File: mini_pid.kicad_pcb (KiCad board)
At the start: 2 copper layers, 68.8 x 63.8 mm, 68 parts, among them P1 PD Mon/Output, P2 Ext. Mod/SetPt Mon, U1 ED2610, U2 OPA2211, U3 LM2940, U4 OPA4227, U5 8DIP, U6 8DIP, U7 OPA2227

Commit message: Layout for old version completed
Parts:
- removed P2: Ext. Mod/SetPt Mon, footprints:Dual-BNC-ARF2136
- added REF**: Via-0.6mm, footprints:Via-0.6mm, F.Cu at (112.8, 72.8)
- added REF**: Via-0.6mm, footprints:Via-0.6mm, F.Cu at (110.7, 103.8)
- added REF**: Via-0.6mm, footprints:Via-0.6mm, F.Cu at (121.8, 90.3)
- added REF**: Via-0.6mm, footprints:Via-0.6mm, F.Cu at (108.6, 98.0)
- added REF**: Via-0.6mm, footprints:Via-0.6mm, F.Cu at (109.9, 98.0)
- added REF**: Via-0.6mm, footprints:Via-0.6mm, F.Cu at (111.4, 99.3)
- added REF**: Via-0.6mm, footprints:Via-0.6mm, F.Cu at (122.9, 92.3)
- added REF**: Via-0.6mm, footprints:Via-0.6mm, F.Cu at (121.9, 94.3)
- added REF**: Via-0.6mm, footprints:Via-0.6mm, F.Cu at (109.5, 90.2)
- added REF**: Via-0.6mm, footprints:Via-0.6mm, F.Cu at (108.8, 93.7)
- added REF**: Via-0.6mm, footprints:Via-0.6mm, F.Cu at (117.0, 85.1)
- added REF**: Via-0.6mm, footprints:Via-0.6mm, F.Cu at (112.3, 70.1)
- added REF**: Via-0.6mm, footprints:Via-0.6mm, F.Cu at (115.8, 85.1)
- added REF**: Via-0.6mm, footprints:Via-0.6mm, F.Cu at (78.9, 90.0)
- added REF**: Via-0.6mm, footprints:Via-0.6mm, F.Cu at (113.2, 69.1)
- added REF**: Via-0.6mm, footprints:Via-0.6mm, F.Cu at (97.0, 100.0)
- added REF**: Via-0.6mm, footprints:Via-0.6mm, F.Cu at (97.7, 99.1)
- added REF**: Via-0.6mm, footprints:Via-0.6mm, F.Cu at (95.9, 99.2)
- added REF**: Via-0.6mm, footprints:Via-0.6mm, F.Cu at (87.8, 96.2)
- added REF**: Via-0.6mm, footprints:Via-0.6mm, F.Cu at (87.6, 97.4)
- added REF**: Via-0.6mm, footprints:Via-0.6mm, F.Cu at (112.0, 103.8)
- added S3: spdt, footprints:CJS-1200TB-SPDT, B.Cu at (120.1, 116.0)
- moved R22 10.8 mm to (114.5, 112.0), turned to 270 degrees
- moved S2 10.6 mm to (129.4, 101.3)
- moved R20 6.00 mm to (113.1, 108.1)
- moved R24 5.73 mm to (131.4, 105.1)
- moved C18 4.58 mm to (125.7, 105.4), turned to 180 degrees
- moved R4 4.51 mm to (127.1, 109.0)
- moved R7 4.28 mm to (124.6, 109.1)
- moved R23 4.27 mm to (125.5, 102.1), turned to 270 degrees
- moved R5 3.57 mm to (129.1, 105.9), turned to 270 degrees
- moved C29 1.31 mm to (89.0, 97.2), turned to 270 degrees
- moved R18 1.21 mm to (87.8, 93.9)
- moved S1 1.20 mm to (110.7, 112.5)
- moved U4 0.59 mm to (119.5, 105.5)
- moved C19 0.28 mm to (113.0, 105.5), turned to 0 degrees
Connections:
- R4 pad 1: Net-(P2-Pad1) -> /ext.mod.input
- U2 pad 9: (no net) -> GND
- U4 pad 1: Net-(R22-Pad2) -> Net-(S3-Pad1)
- U4 pad 2: Net-(R20-Pad2) -> Net-(S3-Pad1)
- U4 pad 3: GND -> Net-(C15-Pad1)
- U4 pad 5: Net-(C15-Pad1) -> GND
- U4 pad 6: Net-(P1-Pad1) -> Net-(R20-Pad2)
- U4 pad 7: Net-(P1-Pad1) -> Net-(R22-Pad2)
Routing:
- net -15V: track 86.2 -> 137.5 mm, vias 4 -> 5
- net Net-(R21-Pad1): track 0.00 -> 41.6 mm, vias 0 -> 1
- net Net-(R18-Pad1): track 3.57 -> 35.4 mm, vias 0 -> 1
- net Net-(R7-Pad2): track 0.00 -> 30.9 mm, vias 0 -> 2
- net /5V: track 0.00 -> 29.5 mm
- net Net-(C11-Pad1): track 0.00 -> 29.5 mm
- net +15V: track 46.9 -> 75.5 mm, vias 0 -> 2
- net Net-(C27-Pad1): track 4.60 -> 31.4 mm
- net Net-(P1-Pad1): track 0.00 -> 25.7 mm
- net Net-(C15-Pad1): track 8.94 -> 32.4 mm
- net Net-(R17-Pad1): track 44.5 -> 59.7 mm
- net Net-(S3-Pad1): track 0.00 -> 14.9 mm, vias 0 -> 1
- net Net-(C20-Pad1): track 34.3 -> 47.5 mm
- net Net-(R6-Pad1): track 33.1 -> 45.8 mm
- net Net-(R10-Pad2): track 31.2 -> 43.9 mm
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- added copper zone on B.Cu, net GND
- added copper zone on F.Cu, net GND
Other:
- board size 68.8 x 63.8 mm -> 67.1 x 63.8 mm

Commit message: Reset board layout
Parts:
- removed REF** (x21): Via-0.6mm, footprints:Via-0.6mm
- added C1: 10uF, Capacitors_SMD:C_0805_HandSoldering, F.Cu at (384.1, 40.0)
- added C31: 1000pF, Capacitors_SMD:C_0805_HandSoldering, F.Cu at (299.2, 145.5)
- added C32: 4700pF, Capacitors_SMD:C_0805_HandSoldering, F.Cu at (307.1, 132.7)
- added C33: 0.022uF, Capacitors_SMD:C_0805_HandSoldering, F.Cu at (323.5, 130.3)
- added C34: 10uF, Capacitors_SMD:C_0805_HandSoldering, F.Cu at (291.2, 155.1)
- added C35: 0.1uF, Capacitors_SMD:C_0805_HandSoldering, F.Cu at (296.8, 151.1)
- added D3: TL4050B51, TO_SOT_Packages_SMD:SOT-23, F.Cu at (264.3, 150.0)
- added D4: TL4050B51, TO_SOT_Packages_SMD:SOT-23, F.Cu at (273.1, 150.0)
- added J1: DB9, footprints:DB9_Throughhole, F.Cu at (397.3, 17.1)
- added P2: Output/Monitor, footprints:Dual-BNC-ARF2136, F.Cu at (343.4, 40.0)
- added P3: Servo In/Ext. Mod, footprints:Dual-BNC-ARF2136, F.Cu at (327.7, 114.3)
- added P4: Output/Monitor, footprints:Dual-BNC-ARF2136, F.Cu at (342.7, 114.3)
- added R25: 10k, Resistors_SMD:R_0805_HandSoldering, F.Cu at (306.6, 138.2)
- added R26: 10k, Resistors_SMD:R_0805_HandSoldering, F.Cu at (311.8, 138.2)
- added R27: 1k, Resistors_SMD:R_0805_HandSoldering, F.Cu at (316.9, 138.2)
- added R28: 10k, Resistors_SMD:R_0805_HandSoldering, F.Cu at (310.5, 143.8)
- added R29: 1k, Resistors_SMD:R_0805_HandSoldering, F.Cu at (327.2, 141.4)
- added R30: 100k, Resistors_SMD:R_0805_HandSoldering, F.Cu at (315.6, 143.8)
- added R31: 10k, Resistors_SMD:R_0805_HandSoldering, F.Cu at (301.8, 151.1)
- added R32: 1k, Resistors_SMD:R_0805_HandSoldering, F.Cu at (322.1, 135.9)
- added R33: 100, Resistors_SMD:R_0805_HandSoldering, F.Cu at (332.4, 135.2)
- added R34: 33k, Resistors_SMD:R_0805_HandSoldering, F.Cu at (322.1, 141.4)
- added R35: 3.3k, Resistors_SMD:R_0805_HandSoldering, F.Cu at (327.2, 135.9)
- added R36: 330, Resistors_SMD:R_0805_HandSoldering, F.Cu at (320.8, 147.0)
- added R37: 12, Resistors_SMD:R_0805_HandSoldering, F.Cu at (312.5, 149.3)
- added R38: 10k, Resistors_SMD:R_0805_HandSoldering, F.Cu at (312.5, 154.9)
- added R39: 1k, Resistors_SMD:R_0805_HandSoldering, F.Cu at (307.0, 155.6)
- added R40: 1k, Resistors_SMD:R_0805_HandSoldering, F.Cu at (317.7, 152.5)
- added R41: 10k, Resistors_SMD:R_0805_HandSoldering, F.Cu at (322.8, 152.5)
- added R42: 10k, Resistors_SMD:R_0805_HandSoldering, F.Cu at (328.0, 147.0)
- added R43: 1k, Resistors_SMD:R_0805_HandSoldering, F.Cu at (338.3, 130.3)
- added R44: 12, Resistors_SMD:R_0805_HandSoldering, F.Cu at (333.1, 140.8)
- added RV3: 10k, footprints:VishaySpectrol536, F.Cu at (263.6, 49.8)
- added RV4: 1k, footprints:VishaySpectrol536, F.Cu at (309.1, 101.3)
- added RV5: 1k, footprints:VishaySpectrol536, F.Cu at (286.4, 101.3)
- added RV6: 10k, footprints:VishaySpectrol536, F.Cu at (263.6, 101.3)
- added S4: spdt, footprints:SPDT-Horizontal, F.Cu at (321.2, 43.2)
- added S5: spdt, footprints:SPDT-Horizontal, F.Cu at (370.1, 94.7)
- added S6: spdt, footprints:SPDT-Horizontal, F.Cu at (356.9, 94.7)
- added S7: spdt, footprints:SPDT-Horizontal, F.Cu at (356.9, 128.2)
- added S8: spdt, footprints:SPDT-Horizontal, F.Cu at (370.1, 128.2)
- added U8: 8DIP, footprints:8_POS_DIP_Switch, F.Cu at (254.2, 139.8)
- added U9: 8DIP, footprints:8_POS_DIP_Switch, F.Cu at (276.4, 139.8)
- C10, C22, C5, C7, C9: footprint Capacitors_SMD:C_0603_HandSoldering -> Capacitors_SMD:C_0805_HandSoldering
- C11, C3, C4: value 10uF -> 0.1uF; footprint Capacitors_SMD:C_0603_HandSoldering -> Capacitors_SMD:C_0805_HandSoldering
- C12: value 0.1uF -> 330pF; footprint Capacitors_SMD:C_0603_HandSoldering -> Capacitors_SMD:C_0805_HandSoldering
- C13, C28: value 0.1uF -> 2200pf; footprint Capacitors_SMD:C_0603_HandSoldering -> Capacitors_SMD:C_0805_HandSoldering
- C14: value 10uF -> 10000pF; footprint Capacitors_SMD:C_0603_HandSoldering -> Capacitors_SMD:C_0805_HandSoldering
- C15: value 15pF -> 0.047uF; footprint Capacitors_SMD:C_0603_HandSoldering -> Capacitors_SMD:C_0805_HandSoldering
- C16: value 22uF -> 1000pF; footprint SMD_Packages:SMD-2512_Pol -> Capacitors_SMD:C_0805_HandSoldering
- C17: value 0.1uF -> 4700pF; footprint Capacitors_SMD:C_0603_HandSoldering -> Capacitors_SMD:C_0805_HandSoldering
- C18: value 0.1uF -> 0.022uF; footprint Capacitors_SMD:C_0603_HandSoldering -> Capacitors_SMD:C_0805_HandSoldering
- C19, C2, C6: value 0.1uF -> 10uF; footprint Capacitors_SMD:C_0603_HandSoldering -> Capacitors_SMD:C_0805_HandSoldering
- C20: value 3.3nF -> 0.1uF; footprint Capacitors_SMD:C_0603_HandSoldering -> Capacitors_SMD:C_0805_HandSoldering
- C21: value 22nF -> 10uF; footprint Capacitors_SMD:C_0603_HandSoldering -> Capacitors_SMD:C_0805_HandSoldering
- C23: value 0.47uF -> 0.1uF; footprint Capacitors_SMD:C_0603_HandSoldering -> Capacitors_SMD:C_0805_HandSoldering
- C24: value 10nF -> 0.1uF; footprint Capacitors_SMD:C_0603_HandSoldering -> Capacitors_SMD:C_0805_HandSoldering
- C25: value 47nF -> 0.1uF; footprint Capacitors_SMD:C_0603_HandSoldering -> Capacitors_SMD:C_0805_HandSoldering
- C26: value 0.22uF -> 0.1uF; footprint Capacitors_SMD:C_0603_HandSoldering -> Capacitors_SMD:C_0805_HandSoldering
- C27: value 10uF -> 330pF; footprint Capacitors_SMD:C_0603_HandSoldering -> Capacitors_SMD:C_0805_HandSoldering
- C29: value 0.1uF -> 10000pF; footprint Capacitors_SMD:C_0603_HandSoldering -> Capacitors_SMD:C_0805_HandSoldering
- C30: value 0.1uF -> 0.047uF; footprint Capacitors_SMD:C_0603_HandSoldering -> Capacitors_SMD:C_0805_HandSoldering
- C8: value 15pF -> 0.1uF; footprint Capacitors_SMD:C_0603_HandSoldering -> Capacitors_SMD:C_0805_HandSoldering
- D1: value S5971 -> TL4050B51; footprint footprints:S5971 -> TO_SOT_Packages_SMD:SOT-23
- P1: value PD Mon/Output -> Servo In/Ext. Mod
- R1: value 3.3k -> 750; footprint Resistors_SMD:R_0603_HandSoldering -> Resistors_SMD:R_0805_HandSoldering
- R10, R21, R5, R7: value 10k -> 1k; footprint Resistors_SMD:R_0603_HandSoldering -> Resistors_SMD:R_0805_HandSoldering
- R11: value 1k -> 100; footprint Resistors_SMD:R_0603_HandSoldering -> Resistors_SMD:R_0805_HandSoldering
- R12: value 100 -> 33k; footprint Resistors_SMD:R_0603_HandSoldering -> Resistors_SMD:R_0805_HandSoldering
- R13: value 33k -> 3.3k; footprint Resistors_SMD:R_0603_HandSoldering -> Resistors_SMD:R_0805_HandSoldering
- R14: value 3.3k -> 330; footprint Resistors_SMD:R_0603_HandSoldering -> Resistors_SMD:R_0805_HandSoldering
- R15: value 330 -> 12; footprint Resistors_SMD:R_0603_HandSoldering -> Resistors_SMD:R_0805_HandSoldering
- R16: value 12 -> 10k; footprint Resistors_SMD:R_0603_HandSoldering -> Resistors_SMD:R_0805_HandSoldering
- R17, R18, R4: footprint Resistors_SMD:R_0603_HandSoldering -> Resistors_SMD:R_0805_HandSoldering
- R19, R20, R6: value 1k -> 10k; footprint Resistors_SMD:R_0603_HandSoldering -> Resistors_SMD:R_0805_HandSoldering
- R2: value 100 -> 750; footprint Resistors_SMD:R_0603_HandSoldering -> Resistors_SMD:R_0805_HandSoldering
- R22: value 1k -> 12; footprint Resistors_SMD:R_0603_HandSoldering -> Resistors_SMD:R_0805_HandSoldering
- R23: value 1k -> 750; footprint Resistors_SMD:R_0603_HandSoldering -> Resistors_SMD:R_0805_HandSoldering
- R24: value 12 -> 750; footprint Resistors_SMD:R_0603_HandSoldering -> Resistors_SMD:R_0805_HandSoldering
- R3: value 3.3k -> 10k; footprint Resistors_SMD:R_0603_HandSoldering -> Resistors_SMD:R_0805_HandSoldering
- R8: value 1k -> 100k; footprint Resistors_SMD:R_0603_HandSoldering -> Resistors_SMD:R_0805_HandSoldering
- R9: value 100k -> 10k; footprint Resistors_SMD:R_0603_HandSoldering -> Resistors_SMD:R_0805_HandSoldering
- RV2: value 10k -> 1k; footprint footprints:Bourns-PV36W104C01B00-trimmer -> footprints:VishaySpectrol536
- S1, S2, S3: footprint footprints:CJS-1200TB-SPDT -> footprints:SPDT-Horizontal
- U2: value OPA2211 -> OPA4227; footprint Housings_SOIC:SOIC-8-1EP_3.9x4.9mm_Pitch1.27mm -> Housings_SOIC:SOIC-14_3.9x8.7mm_Pitch1.27mm
- U3: value LM2940 -> OPA2227; footprint TO_SOT_Packages_SMD:SOT-223 -> Housings_SOIC:SOIC-8_3.9x4.9mm_Pitch1.27mm
- U4: value OPA4227 -> 8DIP; footprint Housings_SOIC:SOIC-14_3.9x8.7mm_Pitch1.27mm -> footprints:8_POS_DIP_Switch
- U6: value 8DIP -> OPA4227; footprint footprints:8_POS_DIP_Switch -> Housings_SOIC:SOIC-14_3.9x8.7mm_Pitch1.27mm
- moved U1 306.1 mm to (422.8, 18.2)
- moved C2 302.5 mm to (415.4, 25.9)
- moved C5 279.6 mm to (399.3, 39.6)
- moved C9 279.2 mm to (375.5, 21.9)
- moved R12 278.4 mm to (365.2, 44.1)
- moved C19 277.3 mm to (375.5, 16.3)
- moved R10 276.3 mm to (372.2, 37.6)
- moved R6 275.7 mm to (371.9, 43.0)
- moved C3 275.6 mm to (389.0, 40.0)
- moved R16 275.3 mm to (359.7, 45.5)
- moved R17 274.3 mm to (364.6, 50.9)
- moved R18 274.1 mm to (359.3, 56.1)
- moved C4 270.0 mm to (394.0, 40.0)
- moved R11 266.8 mm to (359.4, 50.6)
- moved C8 265.4 mm to (372.2, 32.5)
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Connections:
- C11 pad 1: Net-(C11-Pad1) -> GND
- C11 pad 2: GND -> +15V
- C12 pad 1: +15V -> Net-(C12-Pad1)
- C12 pad 2: GND -> Net-(C12-Pad2)
- C13 pad 1: Net-(C11-Pad1) -> Net-(C12-Pad1)
- C13 pad 2: GND -> Net-(C13-Pad2)
- C14 pad 1: +15V -> Net-(C12-Pad1)
- C14 pad 2: GND -> Net-(C14-Pad2)
- C15 pad 1: Net-(C15-Pad1) -> Net-(C12-Pad1)
- C16 pad 1: +9V -> Net-(C12-Pad1)
- C16 pad 2: GND -> Net-(C16-Pad2)
- C17 pad 1: +9V -> Net-(C12-Pad1)
- C17 pad 2: GND -> Net-(C17-Pad2)
- C18 pad 1: GND -> Net-(C12-Pad1)
- C18 pad 2: -15V -> Net-(C18-Pad2)
- C19 pad 1: GND -> Net-(C19-Pad1)
- C19 pad 2: +15V -> /PI Circuit 1/-5V
- C2 pad 1: +9V -> GND
- C2 pad 2: GND -> -15V
- C20 pad 1: Net-(C20-Pad1) -> Net-(C19-Pad1)
- C20 pad 2: Net-(C20-Pad2) -> /PI Circuit 1/-5V
- C21 pad 1: Net-(C20-Pad1) -> /PI Circuit 2/set_point
- C21 pad 2: Net-(C21-Pad2) -> GND
- C22 pad 1: Net-(C20-Pad1) -> /PI Circuit 2/set_point
- C22 pad 2: Net-(C22-Pad2) -> GND
- C23 pad 1: Net-(C20-Pad1) -> GND
- C23 pad 2: Net-(C23-Pad2) -> -15V
- C24 pad 1: Net-(C20-Pad1) -> GND
- C24 pad 2: Net-(C24-Pad2) -> -15V
- C25 pad 1: Net-(C20-Pad1) -> GND
- C25 pad 2: Net-(C25-Pad2) -> +15V
- C26 pad 1: Net-(C20-Pad1) -> GND
- C26 pad 2: Net-(C26-Pad2) -> +15V
- C27 pad 2: GND -> Net-(C27-Pad2)
- C28 pad 2: GND -> Net-(C28-Pad2)
- C29 pad 1: GND -> Net-(C27-Pad1)
- C29 pad 2: -15V -> Net-(C29-Pad2)
- C3 pad 1: +15V -> Net-(C3-Pad1)
- C30 pad 1: GND -> Net-(C27-Pad1)
- C30 pad 2: +15V -> Net-(C30-Pad2)
- C4 pad 1: GND -> +15V
- C4 pad 2: -15V -> Net-(C3-Pad1)
- C5 pad 1: Net-(C5-Pad1) -> Net-(C3-Pad1)
- C5 pad 2: GND -> -15V
- C6 pad 1: +15V -> /PI Circuit 1/set_point
- C6 pad 2: Net-(C5-Pad1) -> GND
- C7 pad 1: Net-(C5-Pad1) -> /PI Circuit 1/set_point
- C7 pad 2: -15V -> GND
- C8 pad 1: Net-(C8-Pad1) -> GND
- C8 pad 2: Net-(C8-Pad2) -> -15V
- D1 pad 1: +9V -> /PI Circuit 1/+5V
- D1 pad 3: Net-(C8-Pad2) -> (no net)
- D2 pad 1: /5V -> GND
- D2 pad 2: GND -> /PI Circuit 1/-5V
- R1 pad 1: Net-(C8-Pad1) -> +15V
- R1 pad 2: Net-(C8-Pad2) -> /PI Circuit 1/+5V
- R16 pad 2: Net-(R10-Pad2) -> Net-(R16-Pad2)
- R17 pad 2: Net-(R10-Pad2) -> Net-(R17-Pad2)
- R18 pad 1: Net-(R18-Pad1) -> Net-(R17-Pad2)
- R18 pad 2: Net-(C20-Pad1) -> Net-(R18-Pad2)
- R19 pad 1: +15V -> Net-(R17-Pad1)
- R19 pad 2: /5V -> Net-(C12-Pad1)
- R2 pad 1: Net-(C15-Pad2) -> /PI Circuit 1/-5V
- R2 pad 2: Net-(C8-Pad1) -> -15V
- R20 pad 1: Net-(R18-Pad1) -> Net-(R20-Pad1)
- R21 pad 1: Net-(R21-Pad1) -> Net-(R20-Pad2)
- R22 pad 1: Net-(R20-Pad2) -> Net-(P2-Pad1)
- R22 pad 2: Net-(R22-Pad2) -> Net-(R21-Pad2)
- R23 pad 1: Net-(R21-Pad2) -> +15V
- R23 pad 2: Net-(R23-Pad2) -> /PI Circuit 2/+5V
- R24 pad 1: Net-(R24-Pad1) -> /PI Circuit 2/-5V
- R24 pad 2: Net-(P1-Pad3) -> -15V
- R3 pad 1: Net-(C15-Pad1) -> Net-(P1-Pad3)
- R3 pad 2: Net-(C15-Pad2) -> Net-(R3-Pad2)
- R4 pad 1: /ext.mod.input -> /PI Circuit 1/set_point
- R4 pad 2: Net-(R4-Pad2) -> Net-(R3-Pad2)
- R5 pad 1: Net-(C11-Pad1) -> Net-(R5-Pad1)
- R5 pad 2: Net-(R4-Pad2) -> Net-(P1-Pad1)
- R6 pad 1: Net-(R6-Pad1) -> Net-(R3-Pad2)
- R6 pad 2: Net-(C15-Pad1) -> /PI Circuit 1/set_point
- R7 pad 1: Net-(R4-Pad2) -> /PI Circuit 1/set_point
- R7 pad 2: Net-(R7-Pad2) -> Net-(R5-Pad1)
- R8 pad 1: Net-(R7-Pad2) -> Net-(R8-Pad1)
- R8 pad 2: Net-(R6-Pad1) -> Net-(R10-Pad2)
- RV1 pad 1: GND -> /PI Circuit 1/-5V
- RV1 pad 2: Net-(C11-Pad1) -> /PI Circuit 1/set_point
- RV1 pad 3: /5V -> /PI Circuit 1/+5V
- RV2 pad 2: Net-(C27-Pad1) -> Net-(R16-Pad1)
- RV2 pad 3: /5V -> Net-(R10-Pad2)
- S1 pad 1: Net-(R22-Pad2) -> Net-(P1-Pad1)
- S1 pad 2: Net-(R21-Pad1) -> Net-(S1-Pad2)
- S1 pad 3: Net-(R18-Pad1) -> /PI Circuit 1/set_point
- S2 pad 1: Net-(R23-Pad2) -> (no net)
- S2 pad 2: Net-(R24-Pad1) -> Net-(C12-Pad1)
- S2 pad 3: Net-(R21-Pad1) -> Net-(R16-Pad2)
- S3 pad 1: Net-(S3-Pad1) -> Net-(R18-Pad2)
- S3 pad 2: Net-(P1-Pad1) -> Net-(S3-Pad2)
- S3 pad 3: /ext.mod.input -> Net-(R17-Pad1)
- U2 pad 1: Net-(C15-Pad1) -> /PI Circuit 1/set_point
- U2 pad 2: Net-(C15-Pad2) -> Net-(R3-Pad2)
- U2 pad 4: -15V -> +15V
- U2 pad 5: GND -> Net-(S1-Pad2)
- U2 pad 6: Net-(C8-Pad2) -> Net-(P2-Pad3)
- U2 pad 7: Net-(C8-Pad1) -> Net-(P2-Pad3)
- U2 pad 8: +15V -> Net-(R18-Pad2)
- U2 pad 9: GND -> Net-(R17-Pad2)
- U3 pad 1: +15V -> Net-(R10-Pad2)
- U3 pad 2: GND -> Net-(R5-Pad1)
- U3 pad 3: +9V -> GND
- U3 pad 4: GND -> -15V
- U4 pad 1: Net-(S3-Pad1) -> Net-(R5-Pad1)
- U4 pad 10: GND -> Net-(R11-Pad1)
- U4 pad 11: -15V -> Net-(R14-Pad1)
- U4 pad 12: Net-(C27-Pad1) -> Net-(R10-Pad1)
- U4 pad 13: Net-(R21-Pad2) -> Net-(R13-Pad1)
- U4 pad 14: Net-(R23-Pad2) -> Net-(R9-Pad1)
- U4 pad 2: Net-(S3-Pad1) -> Net-(R5-Pad1)
- U4 pad 3: Net-(C15-Pad1) -> Net-(R5-Pad1)
- U4 pad 4: +15V -> Net-(R5-Pad1)
- U4 pad 5: GND -> Net-(R5-Pad1)
- U4 pad 6: Net-(R20-Pad2) -> Net-(R5-Pad1)
- U4 pad 7: Net-(R22-Pad2) -> Net-(R5-Pad1)
- U4 pad 8: Net-(R7-Pad2) -> Net-(R5-Pad1)
- U4 pad 9: Net-(R4-Pad2) -> Net-(R15-Pad1)
- U5 pad 1: Net-(R6-Pad1) -> Net-(R16-Pad2)
- U5 pad 10: Net-(R12-Pad1) -> Net-(C15-Pad2)
- U5 pad 11: Net-(R15-Pad1) -> Net-(C18-Pad2)
- U5 pad 12: Net-(R11-Pad1) -> Net-(C14-Pad2)
- U5 pad 13: Net-(R14-Pad1) -> Net-(C17-Pad2)
- U5 pad 14: Net-(R10-Pad1) -> Net-(C13-Pad2)
- U5 pad 15: Net-(R13-Pad1) -> Net-(C16-Pad2)
- U5 pad 16: Net-(R9-Pad1) -> Net-(C12-Pad2)
- U5 pad 2: Net-(R6-Pad1) -> Net-(R16-Pad2)
- U5 pad 3: Net-(R6-Pad1) -> Net-(R16-Pad2)
- U5 pad 4: Net-(R6-Pad1) -> Net-(R16-Pad2)
- U5 pad 5: Net-(R6-Pad1) -> Net-(R16-Pad2)
- U5 pad 6: Net-(R6-Pad1) -> Net-(R16-Pad2)
- U5 pad 7: Net-(R6-Pad1) -> Net-(R16-Pad2)
- U5 pad 8: Net-(R6-Pad1) -> Net-(R16-Pad2)
- U5 pad 9: Net-(R16-Pad1) -> Net-(C12-Pad1)
- U6 pad 1: Net-(R17-Pad1) -> /PI Circuit 2/set_point
- U6 pad 10: Net-(C23-Pad2) -> GND
- U6 pad 11: Net-(C26-Pad2) -> -15V
- U6 pad 12: Net-(C22-Pad2) -> Net-(C34-Pad1)
- U6 pad 13: Net-(C25-Pad2) -> Net-(R42-Pad2)
- U6 pad 14: Net-(C21-Pad2) -> Net-(R43-Pad2)
- U6 pad 2: Net-(R17-Pad1) -> Net-(R25-Pad2)
- U6 pad 3: Net-(R17-Pad1) -> GND
- U6 pad 4: Net-(R17-Pad1) -> +15V
- U6 pad 5: Net-(R17-Pad1) -> Net-(S5-Pad2)
- U6 pad 6: Net-(R17-Pad1) -> Net-(P4-Pad3)
- U6 pad 7: Net-(R17-Pad1) -> Net-(P4-Pad3)
- U6 pad 8: Net-(R17-Pad1) -> Net-(R40-Pad2)
- U6 pad 9: Net-(C20-Pad1) -> Net-(R39-Pad2)
- U7 pad 1: Net-(R18-Pad1) -> Net-(R30-Pad2)
- U7 pad 2: Net-(R17-Pad1) -> Net-(R27-Pad1)
- U7 pad 6: Net-(R6-Pad1) -> Net-(R38-Pad2)
- U7 pad 7: Net-(R10-Pad2) -> Net-(R39-Pad1)
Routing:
- net -15V: track 137.5 -> 0.00 mm, vias 5 -> 0
- net +15V: track 75.5 -> 0.00 mm, vias 2 -> 0
- net Net-(R17-Pad1): track 59.7 -> 0.00 mm, vias 2 -> 0
- net Net-(C20-Pad1): track 47.5 -> 0.00 mm, vias 1 -> 0
- net Net-(R6-Pad1): track 45.8 -> 0.00 mm, vias 1 -> 0
- net Net-(R10-Pad2): track 43.9 -> 0.00 mm
- net Net-(R21-Pad1): track 41.6 -> 0.00 mm, vias 1 -> 0
- net Net-(R18-Pad1): track 35.4 -> 0.00 mm, vias 1 -> 0
- net Net-(C15-Pad1): track 32.4 -> 0.00 mm
- net Net-(C27-Pad1): track 31.4 -> 0.00 mm
- net Net-(R7-Pad2): track 30.9 -> 0.00 mm, vias 2 -> 0
- net /5V: track 29.5 -> 0.00 mm
- net Net-(C11-Pad1): track 29.5 -> 0.00 mm
- net Net-(P1-Pad1): track 25.7 -> 0.00 mm
- net +9V: track 17.9 -> 0.00 mm, vias 2 -> 0
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- removed copper zone on B.Cu, net GND
- removed copper zone on F.Cu, net GND
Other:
- board outline removed
- board text removed: "+15"
- board text removed: "-15"

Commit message: Board connectors placed
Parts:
- C17, P1, R24, RV1, RV2, U1, U5, U6: moved to F.Cu
- S3: footprint footprints:SPDT-Horizontal -> footprints:CJS-1200TB-SPDT
- S4, S5, S6, S8: moved to B.Cu
- S7: footprint footprints:SPDT-Horizontal -> footprints:CJS-1200TB-SPDT; moved to B.Cu
- moved RV2 306.8 mm to (73.7, 204.1), turned to 0 degrees
- moved S4 280.4 mm to (85.4, 195.0), turned to 180 degrees
- moved RV1 280.1 mm to (50.0, 204.1), turned to 0 degrees
- moved S5 279.5 mm to (109.3, 195.0), turned to 180 degrees
- moved P2 279.3 mm to (64.7, 57.8)
- moved U1 274.3 mm to (156.7, 84.3), turned to 180 degrees
- moved S1 270.3 mm to (37.8, 195.0), turned to 180 degrees
- moved S7 269.9 mm to (87.4, 143.4)
- moved S2 260.7 mm to (61.6, 195.0), turned to 180 degrees
- moved P3 247.1 mm to (87.2, 57.8)
- moved P1 246.2 mm to (42.2, 57.8), turned to 0 degrees
- moved S6 245.4 mm to (133.0, 195.1), turned to 180 degrees
- moved J1 244.8 mm to (157.2, 64.7), turned to 180 degrees
- moved P4 237.9 mm to (111.6, 57.8)
- moved S3 234.5 mm to (93.5, 172.8), turned to 180 degrees
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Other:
- board outline added: 329.6 x 208.1 mm

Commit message: PI circuit 1 done
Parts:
- C16, S3, S7: moved to F.Cu
- moved C10 346.8 mm to (45.0, 162.1)
- moved C7 346.7 mm to (37.7, 163.3), turned to 180 degrees
- moved C9 345.5 mm to (48.8, 134.2), turned to 0 degrees
- moved R6 343.8 mm to (46.4, 153.6)
- moved C8 337.8 mm to (60.5, 162.6), turned to 180 degrees
- moved R4 330.3 mm to (40.5, 159.6), turned to 0 degrees
- moved R2 330.2 mm to (48.9, 188.0)
- moved R20 327.8 mm to (59.7, 155.9), turned to 180 degrees
- moved U2 327.4 mm to (52.6, 162.2)
- moved C19 324.9 mm to (99.4, 187.7)
- moved R17 324.9 mm to (60.7, 165.8), turned to 180 degrees
- moved R18 323.4 mm to (56.6, 169.7)
- moved R1 322.7 mm to (42.0, 188.0), turned to 0 degrees
- moved C11 321.4 mm to (56.7, 123.6), turned to 180 degrees
- moved C20 315.9 mm to (59.9, 160.5), turned to 0 degrees
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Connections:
- C19 pad 2: /PI Circuit 1/-5V -> GND
- C20 pad 2: /PI Circuit 1/-5V -> GND
- C34 pad 2: /PI Circuit 2/-5V -> GND
- C35 pad 2: /PI Circuit 2/-5V -> GND
- R28 pad 2: /PI Circuit 2/set_point -> /PI Circuit 2/set_point_mon
- R29 pad 1: /PI Circuit 2/set_point -> /PI Circuit 2/set_point_mon
- R6 pad 2: /PI Circuit 1/set_point -> /PI Circuit 1/set_point_mon
- R7 pad 1: /PI Circuit 1/set_point -> /PI Circuit 1/set_point_mon
- S1 pad 3: /PI Circuit 1/set_point -> /PI Circuit 1/set_point_mon
- S5 pad 3: /PI Circuit 2/set_point -> /PI Circuit 2/set_point_mon
- U2 pad 1: /PI Circuit 1/set_point -> /PI Circuit 1/set_point_mon
- U6 pad 1: /PI Circuit 2/set_point -> /PI Circuit 2/set_point_mon
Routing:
- net Net-(R10-Pad2): track 0.00 -> 164.6 mm
- net Net-(C12-Pad1): track 0.00 -> 143.1 mm, vias 0 -> 2
- net Net-(P1-Pad1): track 0.00 -> 142.6 mm, vias 0 -> 2
- net Net-(P2-Pad3): track 0.00 -> 107.4 mm, vias 0 -> 2
- net Net-(P1-Pad3): track 0.00 -> 100.8 mm
- net Net-(R16-Pad2): track 0.00 -> 99.1 mm, vias 0 -> 2
- net Net-(R21-Pad2): track 0.00 -> 94.3 mm, vias 0 -> 2
- net /PI Circuit 1/+5V: track 0.00 -> 90.3 mm, vias 0 -> 1
- net Net-(C19-Pad1): track 0.00 -> 80.6 mm, vias 0 -> 1
- net /PI Circuit 1/-5V: track 0.00 -> 71.5 mm, vias 0 -> 1
- net Net-(R16-Pad1): track 0.00 -> 70.2 mm
- net Net-(R17-Pad1): track 0.00 -> 65.3 mm, vias 0 -> 2
- net Net-(R20-Pad1): track 0.00 -> 56.4 mm, vias 0 -> 2
- net -15V: track 0.00 -> 49.9 mm
- net /PI Circuit 1/set_point: track 0.00 -> 42.5 mm
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
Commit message: Track routing done.
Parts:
- moved R44 224.6 mm to (118.8, 73.6), turned to 270 degrees
- moved C21 209.7 mm to (127.7, 186.4), turned to 0 degrees
- moved R29 209.4 mm to (118.1, 131.8)
- moved R24 208.6 mm to (113.8, 187.6), turned to 180 degrees
- moved R43 206.6 mm to (132.9, 152.9), turned to 180 degrees
- moved R27 198.5 mm to (118.7, 127.2), turned to 180 degrees
- moved R33 195.1 mm to (138.7, 112.0)
- moved R26 195.0 mm to (117.7, 157.6)
- moved R25 189.8 mm to (117.3, 152.1)
- moved R23 189.7 mm to (121.3, 187.6), turned to 180 degrees
- moved R28 187.1 mm to (123.5, 152.1)
- moved R40 186.2 mm to (132.3, 170.3), turned to 180 degrees
- moved R32 185.6 mm to (138.7, 107.1)
- moved R41 185.2 mm to (140.2, 121.7)
- moved R35 185.1 mm to (144.8, 104.3)
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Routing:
- net Net-(R30-Pad2): track 0.00 -> 166.9 mm
- net Net-(P3-Pad1): track 0.00 -> 158.0 mm
- net Net-(C27-Pad1): track 0.00 -> 147.1 mm, vias 0 -> 1
- net Net-(R38-Pad2): track 0.00 -> 100.6 mm, vias 0 -> 1
- net Net-(P3-Pad3): track 0.00 -> 97.2 mm, vias 0 -> 2
- net /PI Circuit 2/+5V: track 0.00 -> 96.8 mm, vias 0 -> 1
- net Net-(R43-Pad2): track 0.00 -> 90.8 mm, vias 0 -> 2
- net /PI Circuit 2/-5V: track 0.00 -> 80.7 mm, vias 0 -> 1
- net /PI Circuit 2/set_point_mon: track 0.00 -> 80.1 mm, vias 0 -> 2
- net Net-(R38-Pad1): track 0.00 -> 70.1 mm
- net Net-(C34-Pad1): track 0.00 -> 62.7 mm, vias 0 -> 2
- net Net-(S5-Pad2): track 0.00 -> 52.8 mm, vias 0 -> 2
- net /PI Circuit 2/set_point: track 0.00 -> 42.7 mm
- net Net-(S7-Pad2): track 0.00 -> 42.0 mm, vias 0 -> 2
- net Net-(R27-Pad1): track 0.00 -> 40.6 mm
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
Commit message: Added ground planes, fixed unconnected nets.
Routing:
- net -15V: track 57.6 -> 475.3 mm, vias 0 -> 6
- net +15V: track 44.3 -> 384.7 mm, vias 0 -> 9
- net Net-(P4-Pad3): track 1.27 -> 111.2 mm, vias 0 -> 2
- net Net-(R39-Pad1): track 26.3 -> 72.6 mm, vias 0 -> 2
- net /PI Circuit 1/set_point_mon: track 39.4 -> 71.4 mm, vias 0 -> 1
- net /PI Circuit 1/set_point: track 42.5 -> 49.1 mm
- net /PI Circuit 2/set_point_mon: track 80.1 -> 85.8 mm
- net Net-(R16-Pad2): track 99.1 -> 104.2 mm
- added copper zone on B.Cu, net GND
- added copper zone on F.Cu, net GND

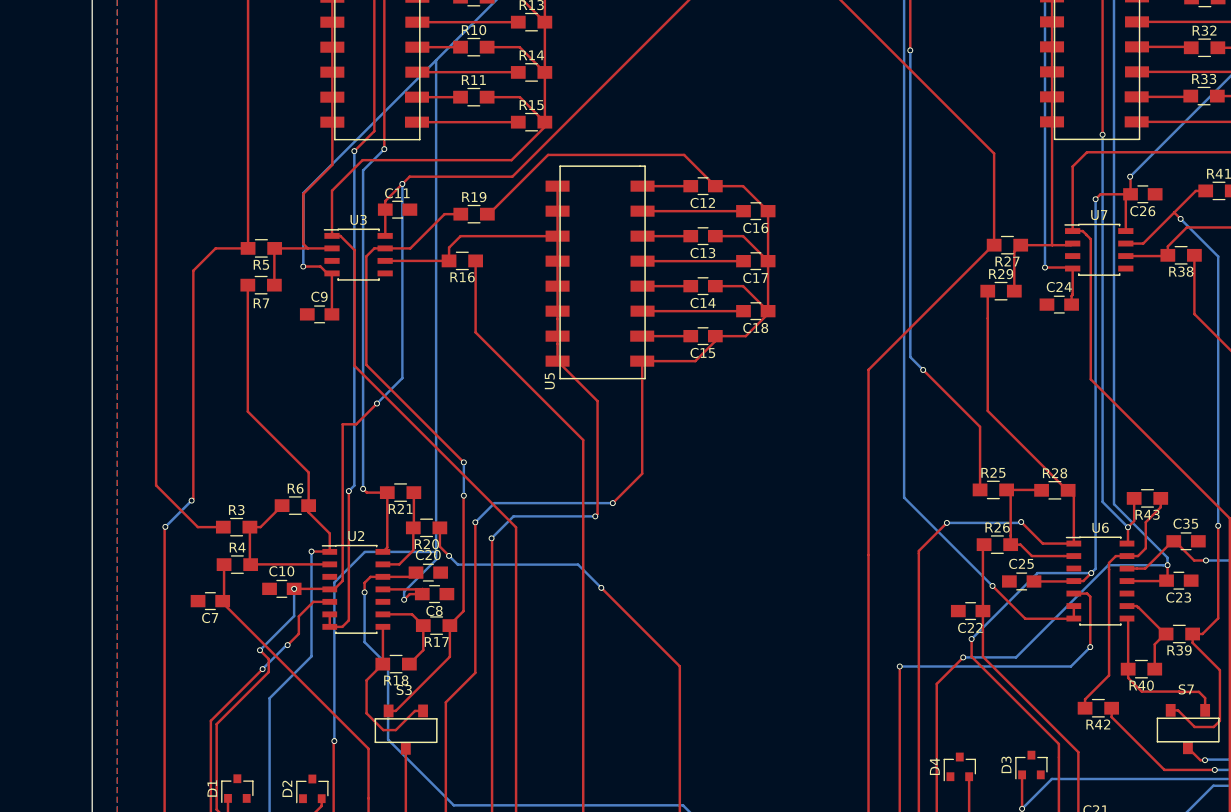
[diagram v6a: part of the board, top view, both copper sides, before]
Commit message: Almost done, but rewiring for optimization
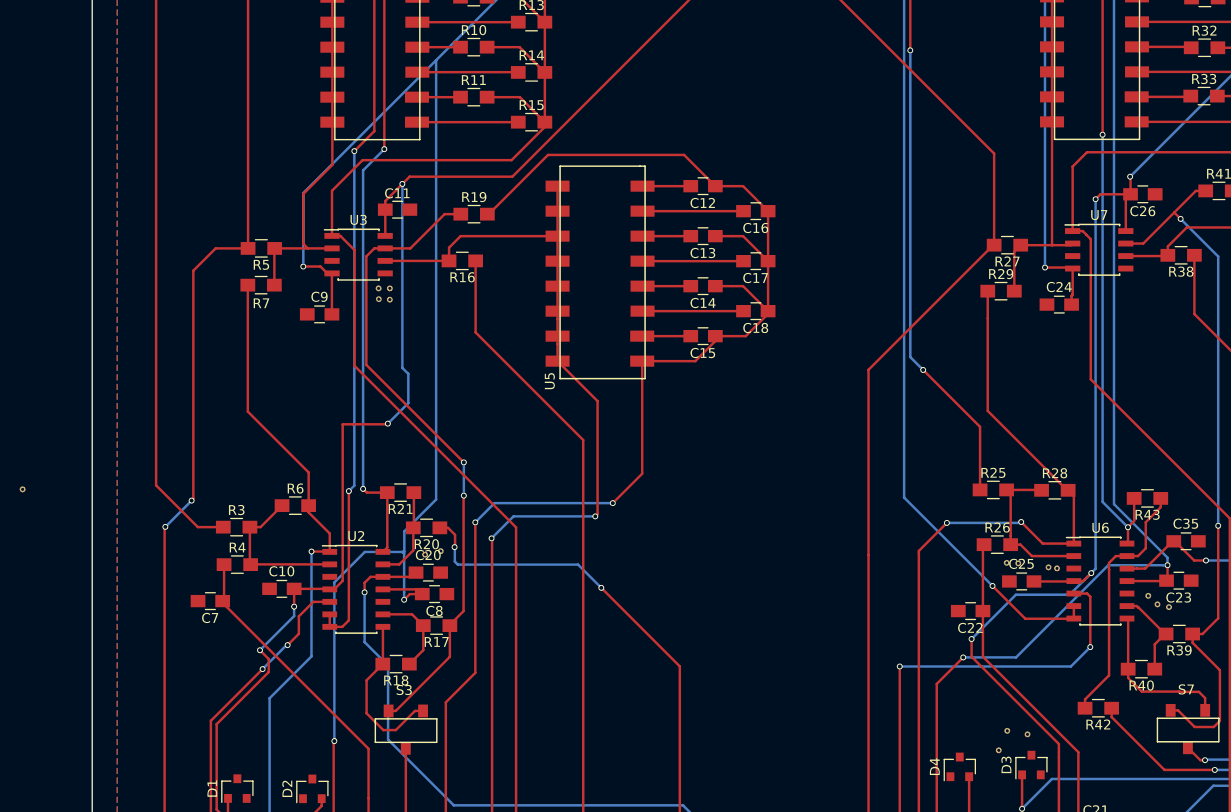
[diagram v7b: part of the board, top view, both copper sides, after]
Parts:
- added REF**: Via-0.6mm, footprints:Via-0.6mm, F.Cu at (118.7, 176.5)
- added REF**: Via-0.6mm, footprints:Via-0.6mm, F.Cu at (122.9, 159.9)
- added REF**: Via-0.6mm, footprints:Via-0.6mm, F.Cu at (118.6, 159.5)
- added REF**: Via-0.6mm, footprints:Via-0.6mm, F.Cu at (119.8, 159.5)
- added REF**: Via-0.6mm, footprints:Via-0.6mm, F.Cu at (123.7, 160.0)
- added REF**: Via-0.6mm, footprints:Via-0.6mm, F.Cu at (135.1, 164.0)
- added REF**: Via-0.6mm, footprints:Via-0.6mm, F.Cu at (134.0, 163.7)
- added REF**: Via-0.6mm, footprints:Via-0.6mm, F.Cu at (133.0, 162.8)
- added REF**: Via-0.6mm, footprints:Via-0.6mm, F.Cu at (18.6, 152.0)
- added REF**: Via-0.6mm, footprints:Via-0.6mm, F.Cu at (120.8, 176.9)
- added REF**: Via-0.6mm, footprints:Via-0.6mm, F.Cu at (117.8, 178.5)
- added REF**: Via-0.6mm, footprints:Via-0.6mm, F.Cu at (61.1, 158.3)
- added REF**: Via-0.6mm, footprints:Via-0.6mm, F.Cu at (59.5, 158.6)
- added REF**: Via-0.6mm, footprints:Via-0.6mm, F.Cu at (56.0, 132.7)
- added REF**: Via-0.6mm, footprints:Via-0.6mm, F.Cu at (54.8, 132.7)
- added REF**: Via-0.6mm, footprints:Via-0.6mm, F.Cu at (54.8, 131.6)
- added REF**: Via-0.6mm, footprints:Via-0.6mm, F.Cu at (56.0, 131.6)
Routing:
- net -15V: track 475.3 -> 472.2 mm
- net +15V: track 384.7 -> 387.0 mm
- net Net-(R20-Pad1): track 56.4 -> 56.9 mm
